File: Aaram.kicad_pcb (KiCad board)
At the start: 2 copper layers, 100 x 100 mm, 52 parts, among them J1 Conn_01x03, J2 Conn_01x02, J3 AC_OUT, J4 SWITCH_IN, J5 5V_OUT, J6 PSU_AC_IN, J8 SPARE_PINS, K1 10A cube relay, K2 10A cube relay, K3 10A cube relay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

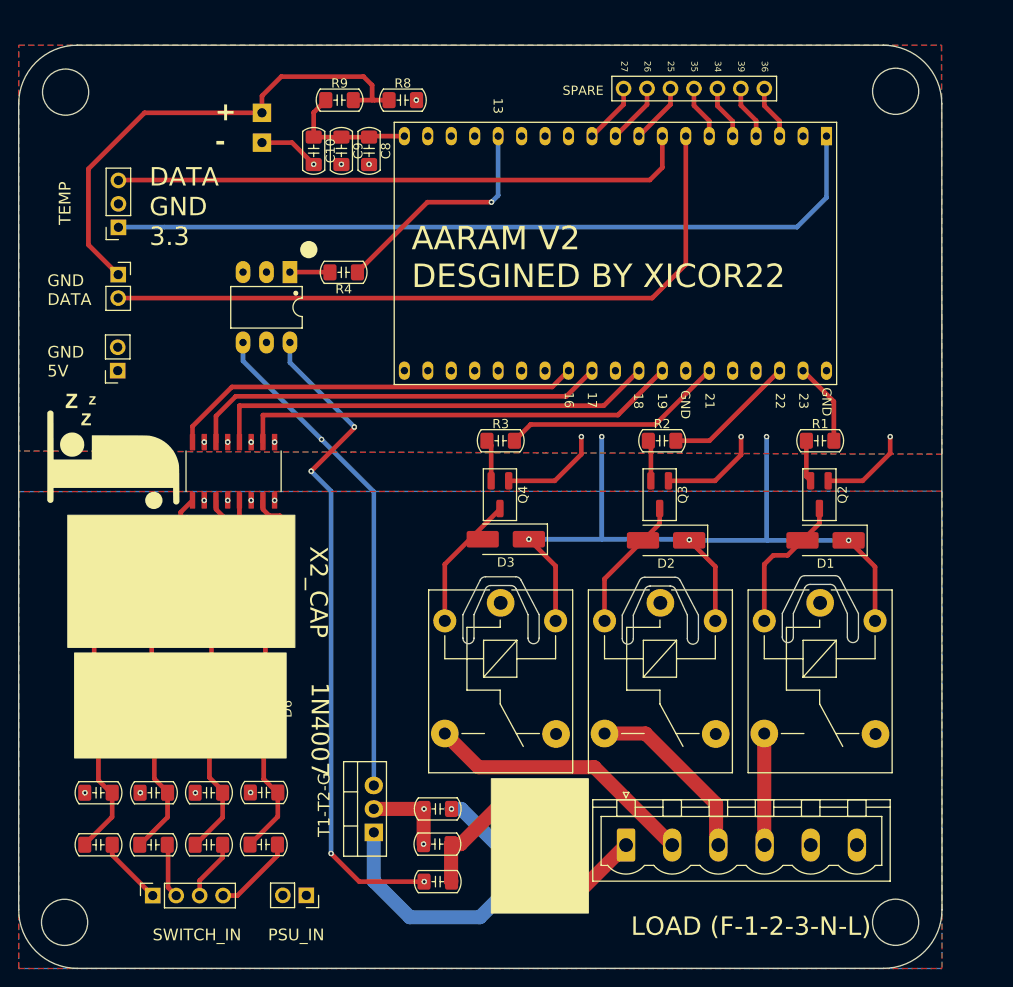
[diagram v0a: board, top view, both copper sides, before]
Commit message: Major Update
1. Added MOVs for high voltage protection
2. Added support for zero cross detection
3. Used SMD components where possible
4. Better AC detection
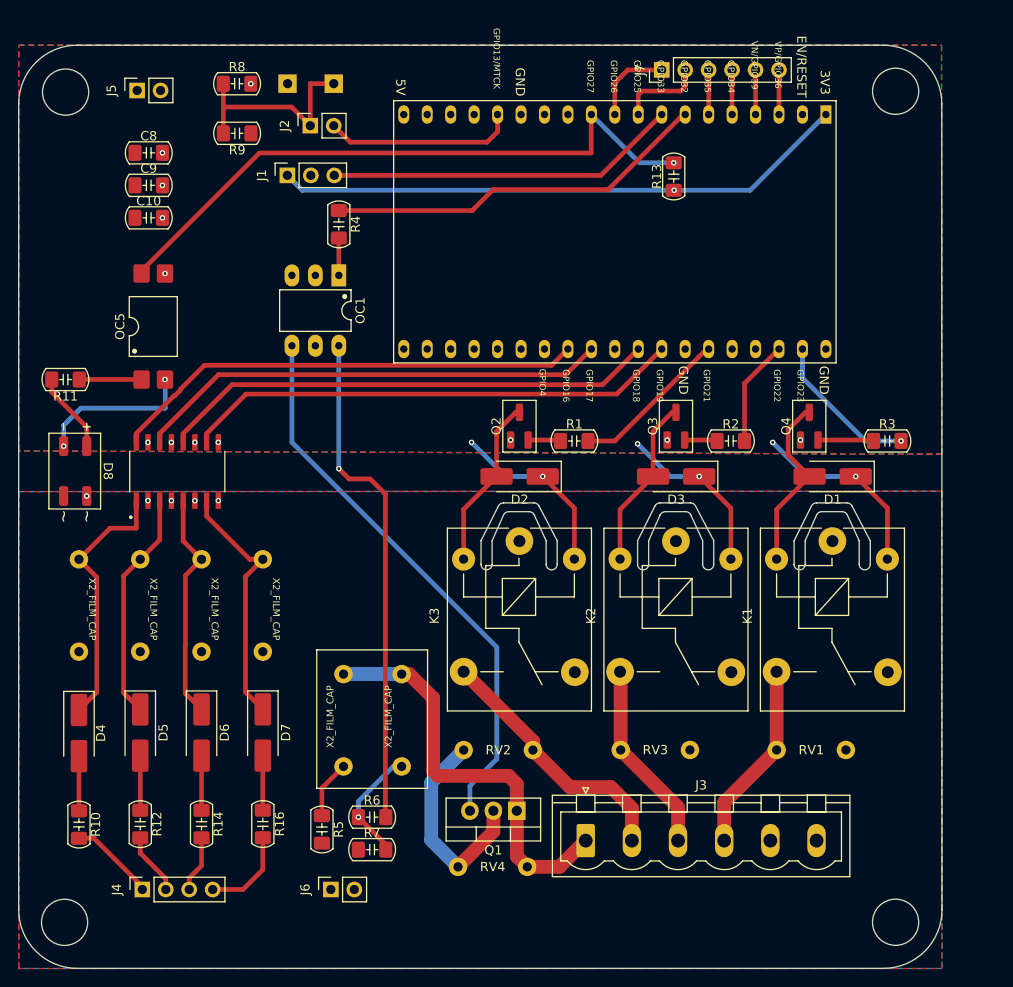
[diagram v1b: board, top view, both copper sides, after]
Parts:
- removed G***: LOGO, LOGO
- removed J8: SPARE_PINS, Connector_PinHeader_2.54mm:PinHeader_1x08_P2.54mm_Vertical
- removed R15, R17: 10K, PCM_Capacitor_SMD_Handsoldering_AKL:C_1206_3216Metric_Pad1.42x1.75mm
- added D8: MB6S, PCM_Diode_SMD_AKL:Diode_Bridge_MBS, F.Cu at (72.8, 79.0)
- added J7: Conn_01x06, Connector_PinHeader_2.54mm:PinHeader_1x06_P2.54mm_Vertical, F.Cu at (136.3, 35.6)
- added OC5: PC817XFP, PCM_Package_DIP_AKL:SMDIP-4_W11.48mm, F.Cu at (81.3, 63.4)
- added RV1: Varistor, Xicor_Custom stuff:Varistor_10D431K, F.Cu at (148.8, 109.2)
- added RV2: Varistor, Xicor_Custom stuff:Varistor_10D431K, F.Cu at (122.4, 109.2)
- added RV3: Varistor, Xicor_Custom stuff:Varistor_10D431K, F.Cu at (131.9, 109.2)
- added RV4: Varistor, Xicor_Custom stuff:Varistor_10D431K, F.Cu at (114.3, 121.9)
- R10, R12, R14, R16: value 1M -> 200K
- R11: value 10K -> 200K
- moved R13 87.3 mm to (137.6, 47.1), turned to 90 degrees
- moved R11 44.9 mm to (71.8, 69.1), turned to 180 degrees
- moved R3 41.9 mm to (160.8, 75.8)
- moved Q4 34.3 mm to (152.3, 74.2), turned to 90 degrees
- moved Q2 33.3 mm to (120.9, 74.2), turned to 90 degrees
- moved J5 30.4 mm to (79.5, 37.8), turned to 90 degrees
- moved R1 26.6 mm to (126.9, 75.8)
- moved J2 26.3 mm to (98.3, 41.6), turned to 90 degrees
- moved C4 24.1 mm to (101.9, 111.0), turned to 90 degrees
- moved C8 23.9 mm to (80.8, 44.6), turned to 0 degrees
- moved C9 21.2 mm to (80.8, 48.1), turned to 0 degrees
- moved K2 20.1 mm to (137.9, 86.6)
- moved D3 19.7 mm to (137.9, 79.6)
- moved C10 19.3 mm to (80.8, 51.6), turned to 0 degrees
- moved J1 19.1 mm to (95.8, 47.0), turned to 90 degrees
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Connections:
- J3 pad 2: LOAD_1 -> LOAD_2
- J3 pad 3: LOAD_2 -> LOAD_1
- Q2 pad 3: Net-(D1-A) -> Net-(D2-A)
- Q3 pad 3: Net-(D2-A) -> Net-(D3-A)
- Q4 pad 3: Net-(D3-A) -> Net-(D1-A)
- R1 pad 2: D3 -> D2
- R11 pad 1: AC_N -> Net-(OC5-Pad1)
- R11 pad 2: Net-(D4-A) -> Net-(D8-+)
- R13 pad 1: AC_N -> +3.3V
- R13 pad 2: Net-(D5-A) -> ZCD
- R14 pad 2: S4 -> S3
- R16 pad 2: S3 -> S4
- R2 pad 2: D2 -> D3
- U1 pad 11: SP2 -> ZCD
- U1 pad 15: T1_Pin -> S2_Pin
- U1 pad 3: SP8 -> SP1
- U1 pad 33: D1 -> D2
- U1 pad 36: D2 -> D3
- U1 pad 37: D3 -> D1
- U1 pad 4: SP7 -> SP2
- U1 pad 7: S2_Pin -> T1_Pin
- U2 pad 5: Net-(D7-K) -> Net-(D6-K)
- U2 pad 7: Net-(D6-K) -> Net-(D7-K)
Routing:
- net ZCD: track 0.00 -> 69.5 mm, vias 0 -> 1
- net S2_Pin: track 76.9 -> 20.8 mm
- net +5V: track 101.3 -> 59.0 mm, vias 5 -> 6
- net GND: track 39.0 -> 0.00 mm, vias 11 -> 12
- net Net-(J2-Pin_1): track 54.7 -> 22.7 mm
- net S1_Pin: track 62.8 -> 38.2 mm
- net +3.3V: track 84.6 -> 62.4 mm, vias 0 -> 1
- net Net-(OC1-Pad6): track 72.4 -> 54.5 mm, vias 4 -> 1
- net Net-(D8--): track 0.00 -> 17.1 mm, vias 0 -> 2
- net T1_Pin: track 25.1 -> 41.8 mm, vias 1 -> 0
- net AC_L: track 9.27 -> 23.0 mm, vias 2 -> 0
- net Net-(C4-Pad1): track 17.2 -> 6.30 mm, vias 1 -> 0
- net Net-(D8-+): track 0.00 -> 8.79 mm
- net LOAD_1: track 29.6 -> 20.9 mm
- net LOAD_2: track 19.9 -> 28.4 mm
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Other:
- outline, holes or cut-outs redrawn
- board text removed: "+ -"
- board text removed: "1N4007"
- board text removed: "AARAM V2 DESGINED BY XICOR22"
- board text removed: "DATA GND 3.3"
- board text removed: "GND 5V"
- board text removed: "GND DATA"
- board text removed: "LOAD (F-1-2-3-N-L)"
- board text removed: "PSU_IN"
- board text removed: "SPARE"
- board text removed: "SWITCH_IN"
- board text removed: "T1-T2-G"
- board text removed: "TEMP"
- board text removed: "X2_CAP"

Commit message: Change footprinnt
Changed transistor footprint
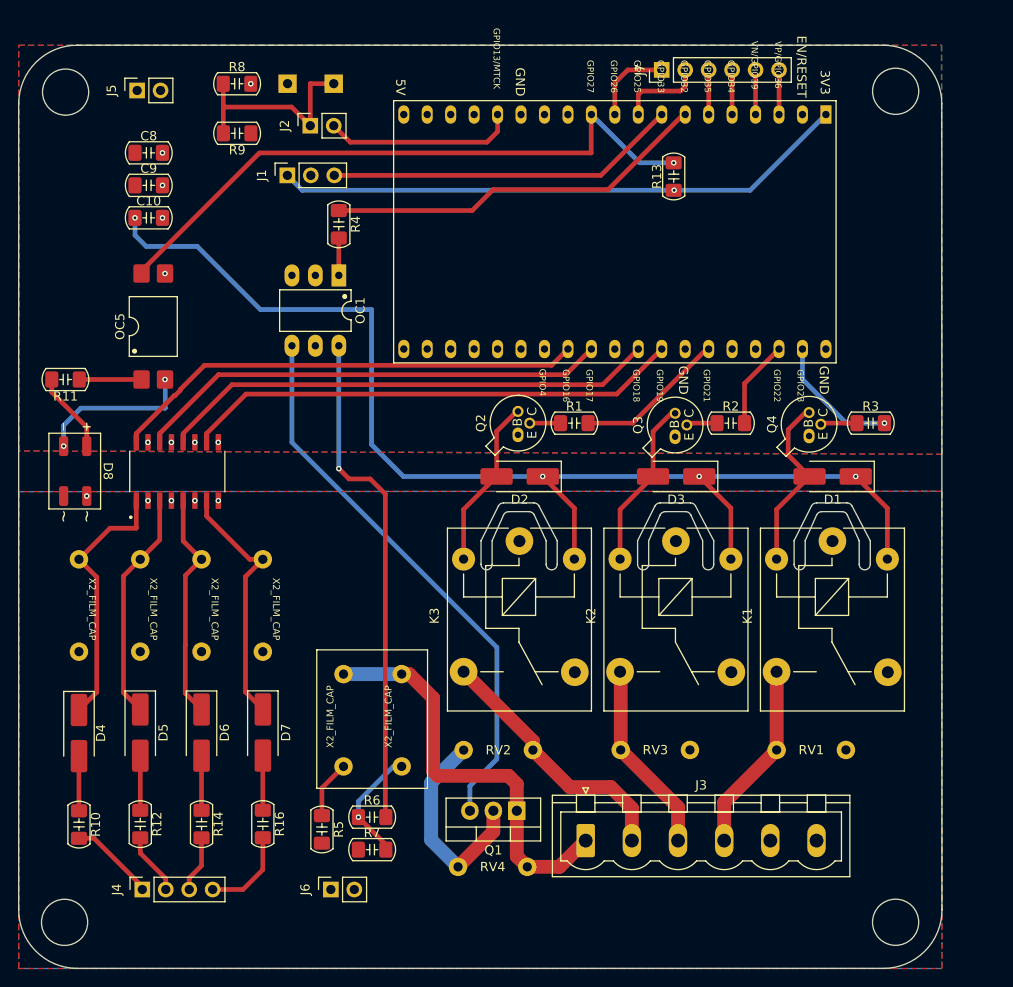
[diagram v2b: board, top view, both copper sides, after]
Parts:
- Q2, Q3, Q4: footprint PCM_Package_TO_SOT_SMD_AKL:SOT-23_BigPads -> PCM_Package_TO_SOT_THT_AKL:TO-18-3_EBC
- moved R3 2.64 mm to (159.0, 73.8)
- moved R1 1.93 mm to (126.9, 73.8)
- moved R2 1.93 mm to (143.8, 73.8)
- moved Q3 1.15 mm to (137.8, 75.3)
- moved Q4 1.06 mm to (152.3, 75.2)
- moved Q2 0.95 mm to (120.8, 75.1)
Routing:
- net +5V: track 59.0 -> 130.4 mm, vias 6 -> 4
- net D1: track 16.6 -> 14.1 mm
- net Net-(Q4-B): track 6.06 -> 3.97 mm
- net D3: track 11.5 -> 9.57 mm
- net D2: track 17.2 -> 16.4 mm
- net GND: vias 12 -> 9
